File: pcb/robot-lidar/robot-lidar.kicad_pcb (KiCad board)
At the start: 2 copper layers, 100 x 100 mm, 48 parts, among them J1 Conn_ARM_SWD_TagConnect_TC2030, J2 YLIDAR X4, J3 Jack-DC, J4 Conn_02x03_Odd_Even, J5 Conn_01x02, J6 Conn_01x02, J7 Conn_01x02, J8 Conn_01x02, SW1 SW_SPST, U1 STM32F429VETx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

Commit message: add linkit
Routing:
- net GND: track 17.5 -> 22.0 mm, vias 19 -> 24
- net PB3-SWO: track 57.7 -> 58.9 mm
- net PA14-SWCLK: track 62.9 -> 61.8 mm
- net Net-(U3-REGOUT): track 5.52 -> 4.71 mm
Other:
- outline, holes or cut-outs redrawn

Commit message: add usb connector on pcb
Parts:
- added J10: Conn_01x18, Connector_PinHeader_2.54mm:PinHeader_1x18_P2.54mm_Vertical, B.Cu at (75.8, 77.4)
- added J11: USB_A, Connector_USB:USB_A_Molex_48037-2200_Horizontal, F.Cu at (91.0, 44.3)
- added J9: Conn_01x18, Connector_PinHeader_2.54mm:PinHeader_1x18_P2.54mm_Vertical, B.Cu at (53.0, 120.6)
- added R13: 10K, Resistor_SMD:R_0603_1608Metric, F.Cu at (92.0, 58.8)
- added R14: 10K, Resistor_SMD:R_0603_1608Metric, F.Cu at (90.0, 58.8)
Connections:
- U1 pad 80: unconnected-(U1-PC12-Pad80) -> UART5_TX
- U1 pad 83: unconnected-(U1-PD2-Pad83) -> UART5_RX
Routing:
- net USB_DP: track 0.00 -> 82.3 mm
- net USB_DM: track 0.00 -> 76.3 mm
- net +5V: track 259.7 -> 320.2 mm, vias 2 -> 4
- net +3V3: track 221.7 -> 281.4 mm, vias 13 -> 14
- net UART5_TX: track 0.00 -> 39.1 mm, vias 0 -> 2
- net UART5_RX: track 0.00 -> 35.0 mm, vias 0 -> 2
- net Net-(D1-A): track 74.7 -> 65.8 mm
- net Net-(J11-D-): track 0.00 -> 2.64 mm
- net Net-(J11-D+): track 0.00 -> 2.64 mm
- net MOTOR_3_B: track 39.8 -> 42.0 mm
- net MOTOR_4_B: track 35.1 -> 35.7 mm
- net GND: vias 24 -> 29

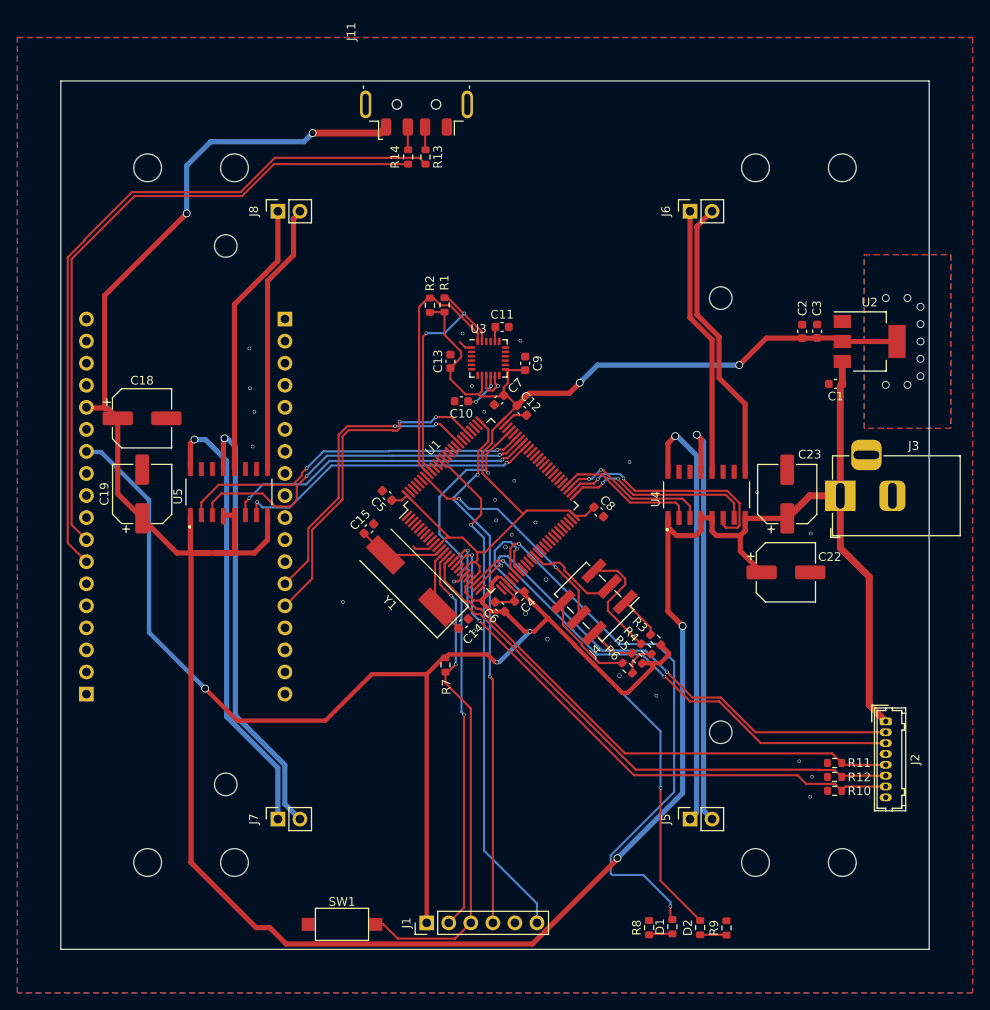
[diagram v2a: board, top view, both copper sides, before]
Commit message: update wiring
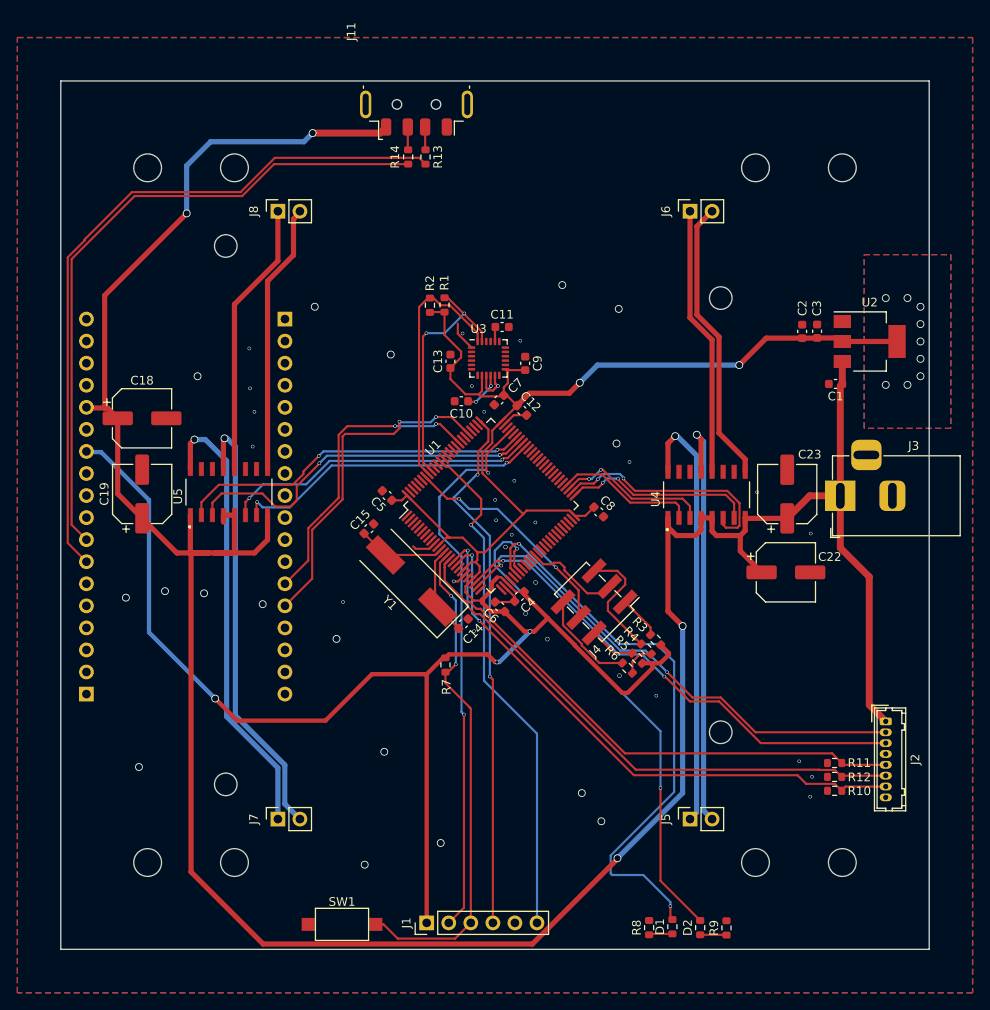
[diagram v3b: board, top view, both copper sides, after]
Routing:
- net GND: track 22.0 -> 23.8 mm, vias 29 -> 46
- net +5V: track 320.2 -> 320.8 mm

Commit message: finish V2
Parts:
- removed C12, C13, C4, C5, C6, C7, C8: 1 uf, Capacitor_SMD:C_0603_1608Metric
- removed D1, D2: LED_Small, Resistor_SMD:R_0603_1608Metric
- removed J10, J9: Conn_01x18, Connector_PinHeader_2.54mm:PinHeader_1x18_P2.54mm_Vertical
- removed J11: USB_A, Connector_USB:USB_A_Molex_48037-2200_Horizontal
- removed R10, R11, R12, R13, R14: 10K, Resistor_SMD:R_0603_1608Metric
- removed R7: 10k, Resistor_SMD:R_0603_1608Metric
- removed R8, R9: 2k, Resistor_SMD:R_0603_1608Metric
- removed SW1: SW_SPST, Button_Switch_SMD:SW_SPST_CK_RS282G05A3
- added J12: Conn_02x20_Odd_Even, Connector_PinHeader_2.54mm:PinHeader_2x20_P2.54mm_Vertical, F.Cu at (55.1, 123.6)
- J3: moved to B.Cu
- U1: value STM32F429VETx -> STM32F103C8Tx; footprint Package_QFP:LQFP-100_14x14mm_P0.5mm -> Package_QFP:LQFP-48_7x7mm_P0.5mm
- moved C18 25.4 mm to (84.2, 83.3), turned to 90 degrees
- moved C19 22.5 mm to (76.9, 83.4)
- moved U5 12.4 mm to (81.3, 94.2)
- moved U1 1.43 mm to (98.7, 100.0)
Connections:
- J2 pad 2: UART4_RX -> UART_RX
- J2 pad 3: UART4_TX -> UART_TX
- R1 pad 2: I2C_SCL -> SCL
- R2 pad 2: I2C_SDA -> SDA
- U1 pad 1: unconnected-(U1-PE2-Pad1) -> +3.3V
- U1 pad 10: GND -> unconnected-(U1-PA0-Pad10)
- U1 pad 11: +3V3 -> unconnected-(U1-PA1-Pad11)
- U1 pad 12: PH0 -> unconnected-(U1-PA2-Pad12)
- U1 pad 13: PH1 -> unconnected-(U1-PA3-Pad13)
- U1 pad 14: RESET -> unconnected-(U1-PA4-Pad14)
- U1 pad 15: M_SCTR -> unconnected-(U1-PA5-Pad15)
- U1 pad 16: DEV_EN -> MOTOR_1_A
- U1 pad 17: M_EN -> MOTOR_1_B
- U1 pad 18: unconnected-(U1-PC3-Pad18) -> MOTOR_2_B
- U1 pad 19: +3V3 -> MOTOR_2_A
- U1 pad 20: GND -> BOOT1
- U1 pad 21: unconnected-(U1-VREF+-Pad21) -> SCL
- U1 pad 22: +3V3 -> SDA
- U1 pad 23: UART4_TX -> GND
- U1 pad 24: UART4_RX -> +3.3V
- U1 pad 27: GND -> unconnected-(U1-PB14-Pad27)
- U1 pad 28: +3V3 -> unconnected-(U1-PB15-Pad28)
- U1 pad 31: Net-(D1-A) -> unconnected-(U1-PA10-Pad31)
- U1 pad 32: Net-(D2-A) -> unconnected-(U1-PA11-Pad32)
- U1 pad 34: unconnected-(U1-PC5-Pad34) -> PA13-SWDIO
- U1 pad 35: unconnected-(U1-PB0-Pad35) -> GND
- U1 pad 36: unconnected-(U1-PB1-Pad36) -> +3.3V
- U1 pad 37: BOOT1 -> PA14-SWCLK
- U1 pad 39: unconnected-(U1-PE8-Pad39) -> PB3-SWO
- U1 pad 42: unconnected-(U1-PE11-Pad42) -> MOTOR_3_A
- U1 pad 43: unconnected-(U1-PE12-Pad43) -> MOTOR_3_B
- U1 pad 44: unconnected-(U1-PE13-Pad44) -> BOOT0
- U1 pad 45: unconnected-(U1-PE14-Pad45) -> MOTOR_4_A
- U1 pad 46: unconnected-(U1-PE15-Pad46) -> MOTOR_4_B
- U1 pad 47: unconnected-(U1-PB10-Pad47) -> GND
- U1 pad 48: unconnected-(U1-PB11-Pad48) -> +3.3V
- U1 pad 5: unconnected-(U1-PE6-Pad5) -> PH0
- U1 pad 6: unconnected-(U1-VBAT-Pad6) -> PH1
- U1 pad 7: unconnected-(U1-PC13-Pad7) -> RESET
- U1 pad 8: unconnected-(U1-PC14-Pad8) -> GND
- U1 pad 9: unconnected-(U1-PC15-Pad9) -> +3.3V
- U3 pad 23: I2C_SCL -> SCL
- U3 pad 24: I2C_SDA -> SDA
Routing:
- net SCL: track 0.00 -> 133.2 mm, vias 0 -> 3
- net SDA: track 0.00 -> 127.5 mm, vias 0 -> 2
- net +3V3: track 281.4 -> 175.9 mm
- net UART_RX: track 0.00 -> 102.4 mm, vias 0 -> 4
- net UART_TX: track 0.00 -> 100.6 mm, vias 0 -> 4
- net USB_DP: track 82.3 -> 0.00 mm
- net USB_DM: track 76.3 -> 0.00 mm
- net Net-(D1-A): track 65.8 -> 0.00 mm, vias 2 -> 0
- net Net-(D2-A): track 58.7 -> 0.00 mm, vias 2 -> 0
- net UART4_RX: track 57.7 -> 0.00 mm, vias 2 -> 0
- net UART4_TX: track 57.1 -> 0.00 mm, vias 2 -> 0
- net M_SCTR: track 62.4 -> 110.5 mm
- net M_EN: track 65.3 -> 110.9 mm
- net +5V: track 320.8 -> 278.2 mm, vias 4 -> 3
- net DEV_EN: track 65.1 -> 107.3 mm, vias 2 -> 0
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
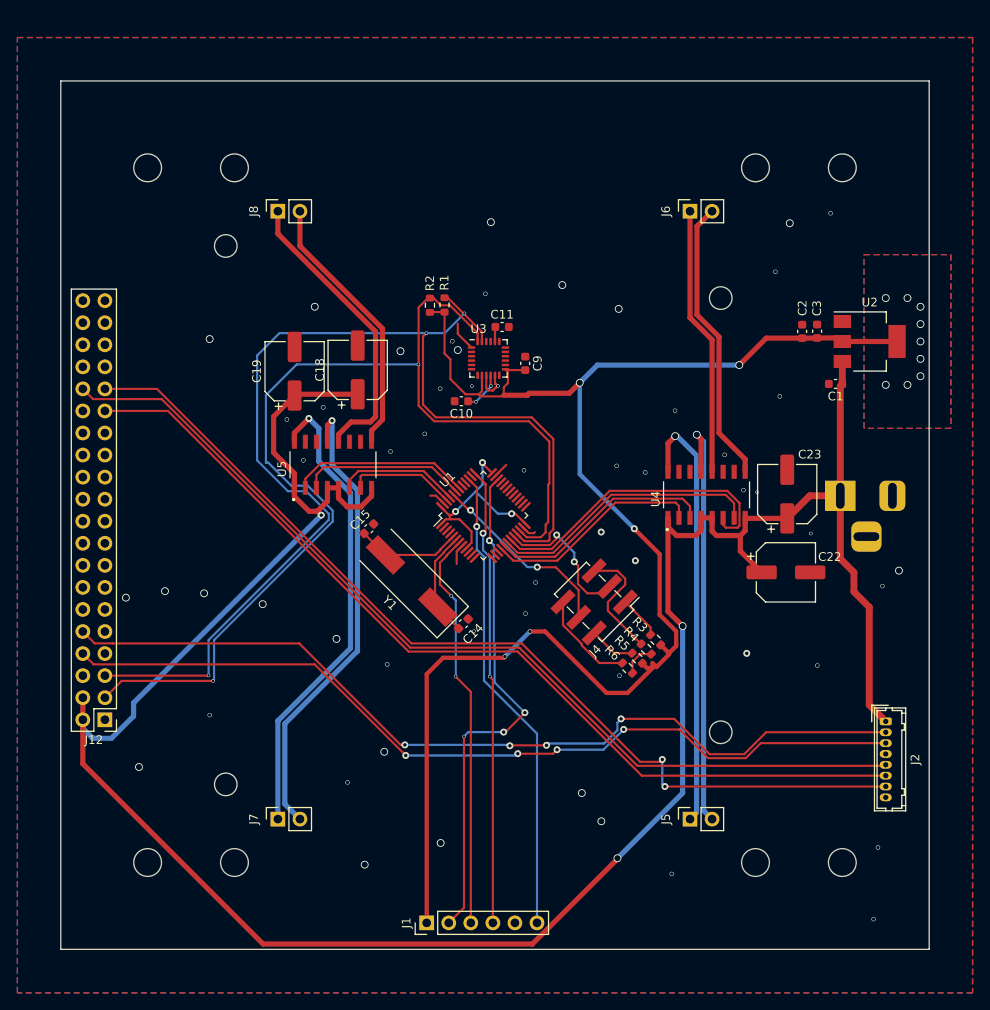
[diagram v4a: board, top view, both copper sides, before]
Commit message: rewire i2c
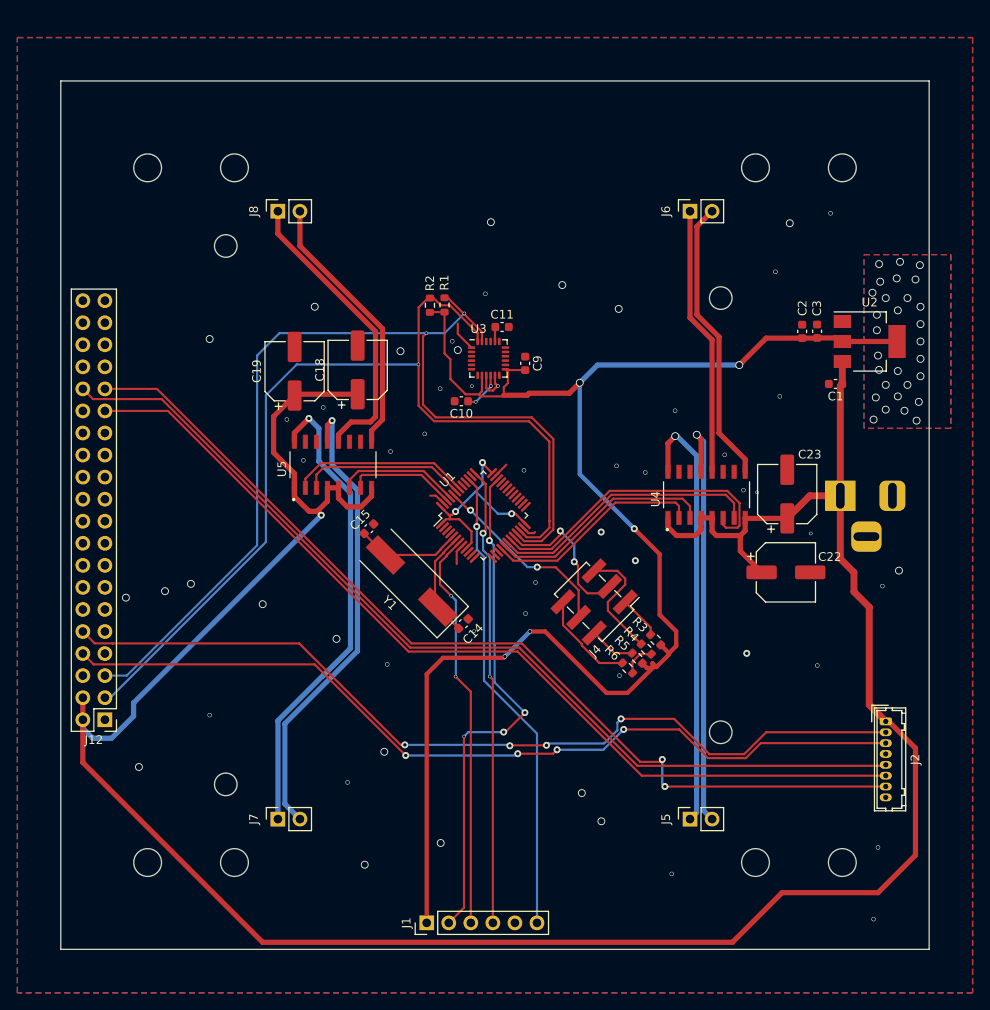
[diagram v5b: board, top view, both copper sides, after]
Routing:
- net SCL: track 133.2 -> 119.1 mm, vias 3 -> 2
- net SDA: track 127.5 -> 114.0 mm, vias 2 -> 1
- net +5V: track 278.2 -> 286.4 mm, vias 3 -> 1
- net BOOT1: track 17.2 -> 18.1 mm
- net +3V3: vias 14 -> 34
